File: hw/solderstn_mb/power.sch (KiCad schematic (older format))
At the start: 63 parts, among them Q301 Si4497DY, Q302 DMG1012T, U301 TPS54332DDA, U302 TLV1117LV30DCY, U303 TLV1117LV30DCY, U304 TLV1117LV30DCY, U305 AP22811AW5

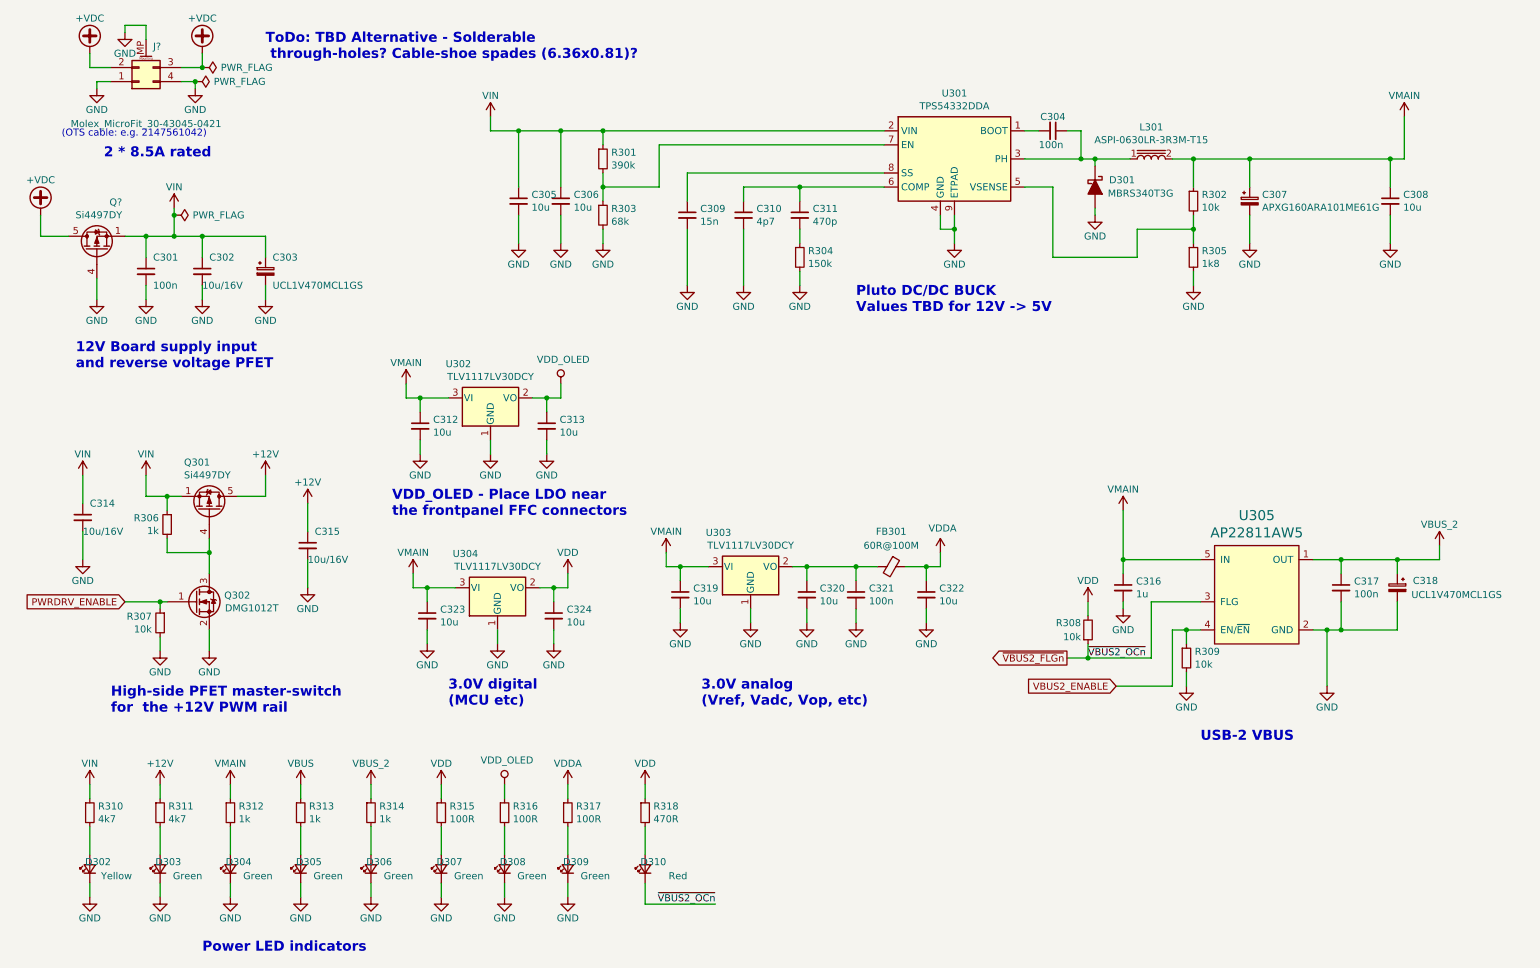
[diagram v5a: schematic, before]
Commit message: Updated display-board sch & PCB with optional left-hand rotary encoder instead of pwrbtn. Printed MB schematic updates PDF for 20-08-21
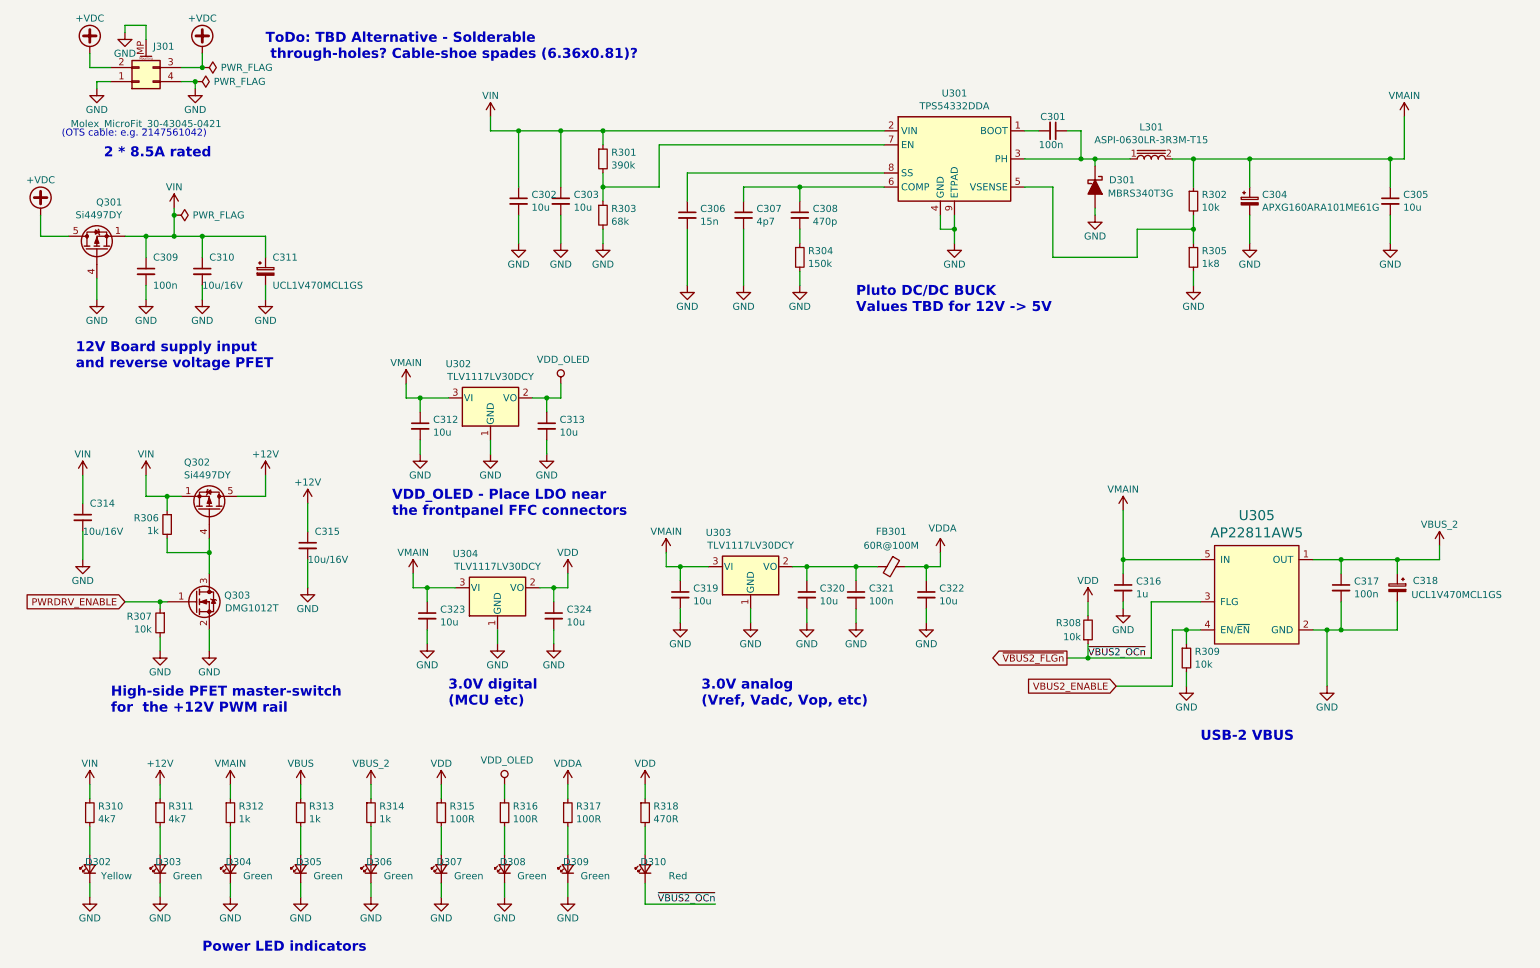
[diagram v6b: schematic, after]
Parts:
- gave numbers to parts that had none: 2
- renumbered C304 to C301, C305 to C302, C306 to C303, C307 to C304, C308 to C305, C309 to C306, C310 to C307, C311 to C308, C301 to C309, C302 to C310, C303 to C311, Q301 to Q302, Q302 to Q303

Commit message: Corrected several ERC issues. Re-annotated & assigned all footprints except 32k xtal (will prob. replace with RTC module anyway)
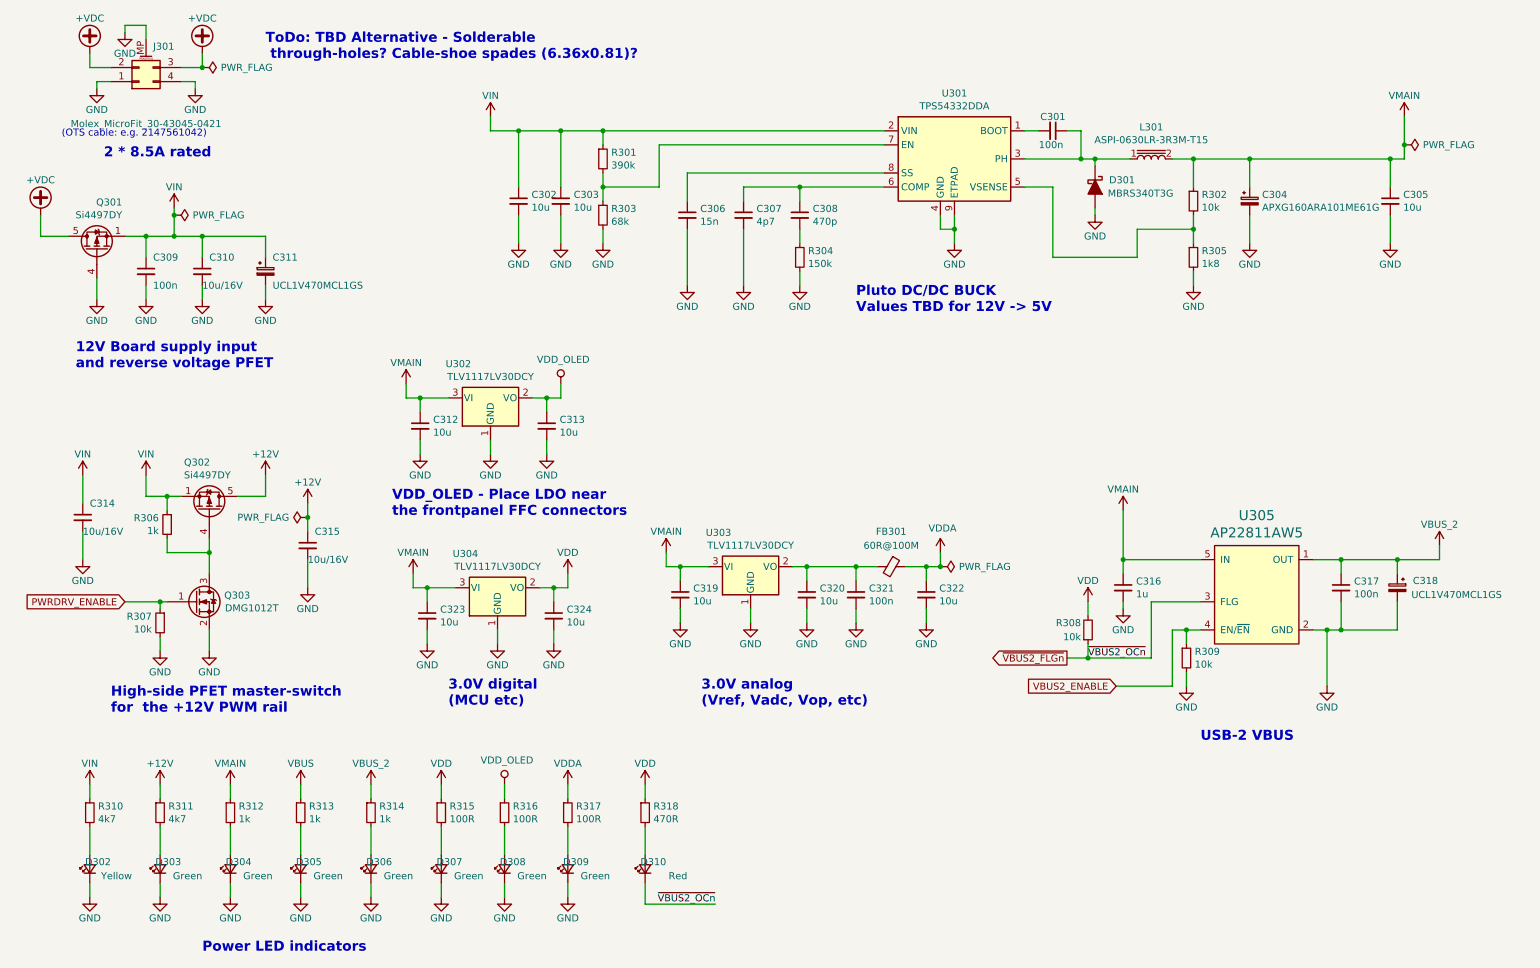
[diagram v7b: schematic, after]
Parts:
- C301, C302, C303, C305, C309, C310, C312, C313, C314, C315, C316, C317, C319, C320, C321, C322, C323, C324: footprint (none) -> Capacitor_SMD:C_0603_1608Metric
- C306, C307, C308: footprint (none) -> Capacitor_SMD:C_0402_1005Metric
- D302, D303, D304, D305, D306, D307, D308, D309, D310: footprint (none) -> LED_SMD:LED_0603_1608Metric
- FB301: footprint (none) -> Inductor_SMD:L_0603_1608Metric
- Q303: footprint bobs:SOT-523 -> customlib_mj_fp:SOT-523
- R301, R302, R303, R304, R305, R306, R307, R308, R309, R310, R311, R312, R313, R314, R315, R316, R317, R318: footprint (none) -> Resistor_SMD:R_0603_1608Metric

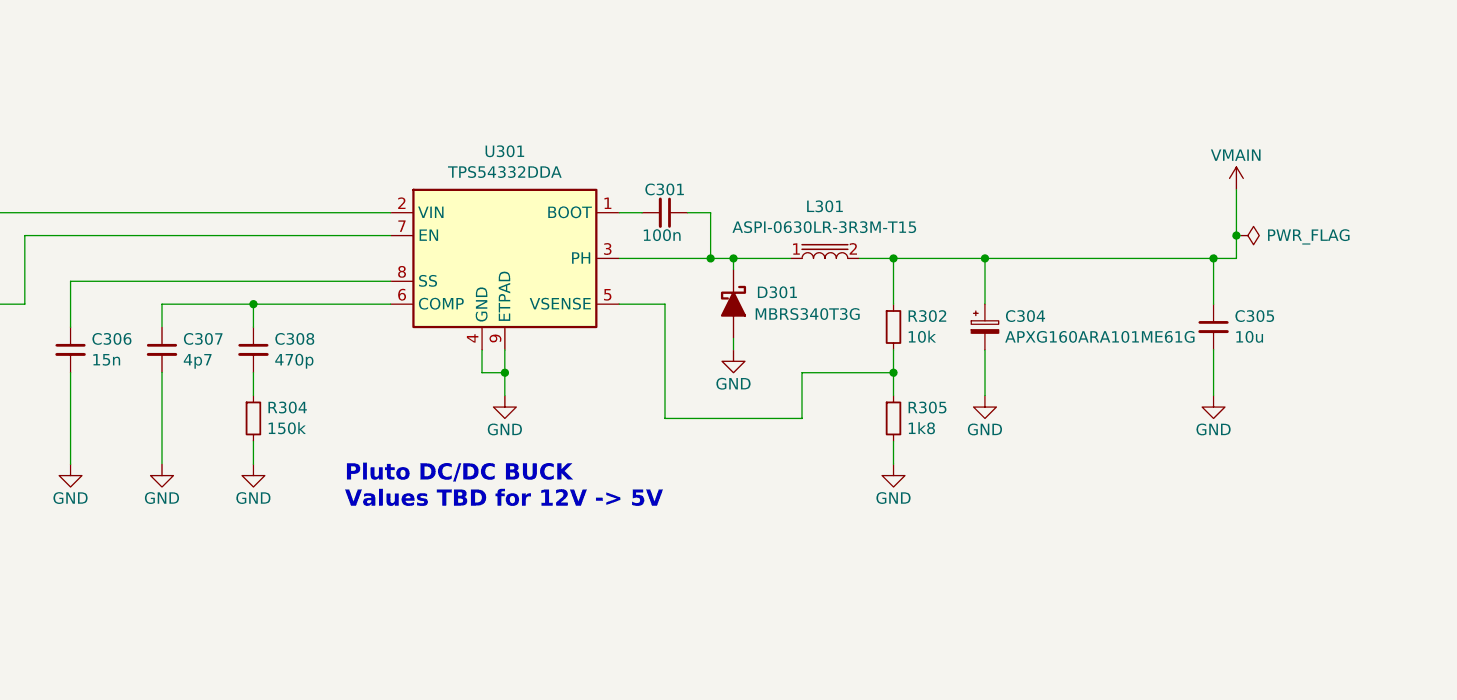
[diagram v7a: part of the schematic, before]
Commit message: Updated DC/DC buck values after testing TPS54332 in TI WebBench. New MB printed schematics.
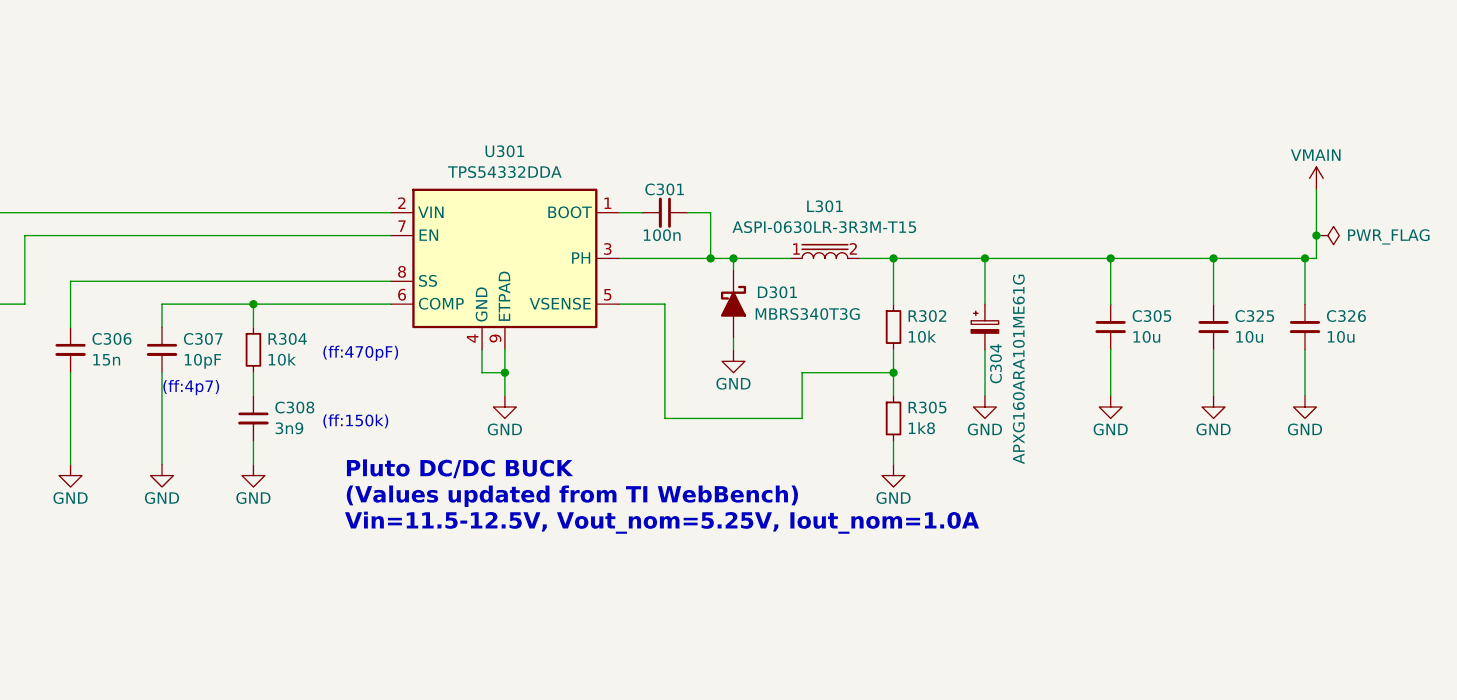
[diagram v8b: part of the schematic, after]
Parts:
- added C325, C326: 10u, Capacitor_SMD:C_0603_1608Metric, symbol Device:C_Small
- C307: value 4p7 -> 10pF
- C308: value 470p -> 3n9
- R304: value 150k -> 10k
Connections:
- net GND: now also C308.2, C325.2, C326.2; no longer R304.2
- net VMAIN: now also C325.1, C326.1
- net at C307.1, U301.6 (COMP): now also R304.1; no longer C308.1
- new net: C308.1, R304.2
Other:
- note added: "(ff:150k)"
- note added: "(ff:470pF)"
- note added: "(ff:4p7)"
- note added: "Pluto DC/DC BUCK\n(Values updated from TI WebBench)\nVin=11.5-12.5V, Vout_nom=5.25V, Iout_nom=1.0A"
- note removed: "Pluto DC/DC BUCK\nValues TBD for 12V -> 5V"
- moved on the sheet: C305, C308, R304
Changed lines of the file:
@@
 P 5650 2050
 F 0 "C307" H 5742 2096 50  0000 L CNN
-F 1 "4p7" H 5742 2005 50  0000 L CNN
+F 1 "10pF" H 5742 2005 50  0000 L CNN
 F 2 "Capacitor_SMD:C_0402_1005Metric" H 5650 2050 50  0001 C CNN
 F 3 "~" H 5650 2050 50  0001 C CNN
@@
 $EndComp
 $Comp
-L Device:C_Small C308
-U 1 1 5F4831B5
+L Device:R_Small R304
+U 1 1 5F483485
 P 6050 2050
-F 0 "C308" H 6142 2096 50  0000 L CNN
-F 1 "470p" H 6142 2005 50  0000 L CNN
-F 2 "Capacitor_SMD:C_0402_1005Metric" H 6050 2050 50  0001 C CNN
+F 0 "R304" H 6109 2096 50  0000 L CNN
+F 1 "10k" H 6109 2005 50  0000 L CNN
+F 2 "Resistor_SMD:R_0603_1608Metric" H 6050 2050 50  0001 C CNN
 F 3 "~" H 6050 2050 50  0001 C CNN
 	1    6050 2050
-	1    0    0    -1
-$EndComp
-$Comp
-L Device:R_Small R304
-U 1 1 5F483485
-P 6050 2350
-F 0 "R304" H 6109 2396 50  0000 L CNN
-F 1 "150k" H 6109 2305 50  0000 L CNN
-F 2 "Resistor_SMD:R_0603_1608Metric" H 6050 2350 50  0001 C CNN
-F 3 "~" H 6050 2350 50  0001 C CNN
-	1    6050 2350
 	1    0    0    -1
 $EndComp
@@
 	5650 1850 5650 1950
 Connection ~ 6050 1850
-Wire Wire Line
-	6050 2150 6050 2250
 Wire Wire Line
 	6650 1750 5250 1750
@@
 U 1 1 5F497049
 P 9250 1950
-F 0 "C304" H 9338 1996 50  0000 L CNN
-F 1 "APXG160ARA101ME61G" H 9338 1905 50  0000 L CNN
+F 0 "C304" V 9300 1700 50  0000 L CNN
+F 1 "APXG160ARA101ME61G" V 9400 1350 50  0000 L CNN
 F 2 "Capacitor_SMD:CP_Elec_5x5.8" H 9250 1950 50  0001 C CNN
 F 3 "https://www.mouser.se/datasheet/2/420/United-Chemi-Con-775864.pdf" H 9250 1950 50  0001 C CNN
@@
 L Device:C_Small C305
 U 1 1 5F497D32
-P 10250 1950
-F 0 "C305" H 10342 1996 50  0000 L CNN
-F 1 "10u" H 10342 1905 50  0000 L CNN
-F 2 "Capacitor_SMD:C_0603_1608Metric" H 10250 1950 50  0001 C CNN
-F 3 "~" H 10250 1950 50  0001 C CNN
-	1    10250 1950
+P 9800 1950
+F 0 "C305" H 9892 1996 50  0000 L CNN
+F 1 "10u" H 9892 1905 50  0000 L CNN
+F 2 "Capacitor_SMD:C_0603_1608Metric" H 9800 1950 50  0001 C CNN
+F 3 "~" H 9800 1950 50  0001 C CNN
+	1    9800 1950
 	1    0    0    -1
 $EndComp
@@
 L power:GND #PWR0316
 U 1 1 5F499E9F
-P 10250 2250
-F 0 "#PWR0316" H 10250 2000 50  0001 C CNN
-F 1 "GND" H 10250 2100 50  0000 C CNN
-F 2 "" H 10250 2250 50  0001 C CNN
-F 3 "" H 10250 2250 50  0001 C CNN
-	1    10250 2250
+P 9800 2250
+F 0 "#PWR0316" H 9800 2000 50  0001 C CNN
+F 1 "GND" H 9800 2100 50  0000 C CNN
+F 2 "" H 9800 2250 50  0001 C CNN
+F 3 "" H 9800 2250 50  0001 C CNN
+	1    9800 2250
 	1    0    0    -1
 $EndComp
@@
 L customlib_mj:VMAIN #PWR0307
 U 1 1 5F4A6151
-P 10350 1350
-F 0 "#PWR0307" H 10350 1200 50  0001 C CNN
-F 1 "VMAIN" H 10350 1500 50  0000 C CNN
-F 2 "" H 10350 1350 50  0001 C CNN
-F 3 "" H 10350 1350 50  0001 C CNN
-	1    10350 1350
+P 10700 1350
+F 0 "#PWR0307" H 10700 1200 50  0001 C CNN
+F 1 "VMAIN" H 10700 1500 50  0000 C CNN
+F 2 "" H 10700 1350 50  0001 C CNN
+F 3 "" H 10700 1350 50  0001 C CNN
+	1    10700 1350
 	1    0    0    -1
 $EndComp
@@
 	8700 1650 8850 1650
 Wire Wire Line
-	10350 1650 10350 1550
+	10700 1650 10700 1550
 Wire Wire Line
 	8850 1850 8850 1650
@@
 Connection ~ 9250 1650
 Wire Wire Line
-	9250 1650 10250 1650
+	9250 1650 9800 1650
 Wire Wire Line
 	9250 2250 9250 2050
 Wire Wire Line
-	10250 2250 10250 2050
-Wire Wire Line
-	10250 1850 10250 1650
-Connection ~ 10250 1650
-Wire Wire Line
-	10250 1650 10350 1650
-Text Notes 6450 2750 0    71   ~ 14
-Pluto DC/DC BUCK\nValues TBD for 12V -> 5V
+	9800 2250 9800 2050
+Wire Wire Line
+	9800 1850 9800 1650
+Text Notes 6450 2850 0    71   ~ 14
+Pluto DC/DC BUCK\n(Values updated from TI WebBench)\nVin=11.5-12.5V, Vout_nom=5.25V, Iout_nom=1.0A
 $Comp
 L customlib_mj:TLV1117LV30DCY U304
@@
 L power:PWR_FLAG #FLG0302
 U 1 1 5F505787
-P 10350 1550
-F 0 "#FLG0302" H 10350 1625 50  0001 C CNN
-F 1 "PWR_FLAG" V 10350 1866 50  0000 C CNN
-F 2 "" H 10350 1550 50  0001 C CNN
-F 3 "~" H 10350 1550 50  0001 C CNN
-	1    10350 1550
+P 10700 1550
+F 0 "#FLG0302" H 10700 1625 50  0001 C CNN
+F 1 "PWR_FLAG" V 10700 1866 50  0000 C CNN
+F 2 "" H 10700 1550 50  0001 C CNN
+F 3 "~" H 10700 1550 50  0001 C CNN
+	1    10700 1550
 	0    1    1    0
 $EndComp
-Connection ~ 10350 1550
-Wire Wire Line
-	10350 1550 10350 1350
+Connection ~ 10700 1550
+Wire Wire Line
+	10700 1550 10700 1350
 $Comp
 L power:PWR_FLAG #FLG0304
@@
 Wire Wire Line
 	2550 4200 2550 4300
+Text Notes 5650 2250 0    50   ~ 0
+(ff:4p7)
+Text Notes 6350 2400 0    50   ~ 0
+(ff:150k)
+$Comp
+L Device:C_Small C308
+U 1 1 5F4831B5
+P 6050 2350
+F 0 "C308" H 6142 2396 50  0000 L CNN
+F 1 "3n9" H 6142 2305 50  0000 L CNN
+F 2 "Capacitor_SMD:C_0402_1005Metric" H 6050 2350 50  0001 C CNN
+F 3 "~" H 6050 2350 50  0001 C CNN
+	1    6050 2350
+	1    0    0    -1
+$EndComp
+Text Notes 6350 2100 0    50   ~ 0
+(ff:470pF)
+Wire Wire Line
+	6050 2250 6050 2150
+Connection ~ 9800 1650
+$Comp
+L Device:C_Small C325
+U 1 1 5F4B09C1
+P 10250 1950
+F 0 "C325" H 10342 1996 50  0000 L CNN
+F 1 "10u" H 10342 1905 50  0000 L CNN
+F 2 "Capacitor_SMD:C_0603_1608Metric" H 10250 1950 50  0001 C CNN
+F 3 "~" H 10250 1950 50  0001 C CNN
+	1    10250 1950
+	1    0    0    -1
+$EndComp
+$Comp
+L power:GND #PWR0373
+U 1 1 5F4B09CB
+P 10250 2250
+F 0 "#PWR0373" H 10250 2000 50  0001 C CNN
+F 1 "GND" H 10250 2100 50  0000 C CNN
+F 2 "" H 10250 2250 50  0001 C CNN
+F 3 "" H 10250 2250 50  0001 C CNN
+	1    10250 2250
+	1    0    0    -1
+$EndComp
+Wire Wire Line
+	10250 2250 10250 2050
+Wire Wire Line
+	10250 1850 10250 1650
+$Comp
+L Device:C_Small C326
+U 1 1 5F4BEE07
+P 10650 1950
+F 0 "C326" H 10742 1996 50  0000 L CNN
+F 1 "10u" H 10742 1905 50  0000 L CNN
+F 2 "Capacitor_SMD:C_0603_1608Metric" H 10650 1950 50  0001 C CNN
+F 3 "~" H 10650 1950 50  0001 C CNN
+	1    10650 1950
+	1    0    0    -1
+$EndComp
+$Comp
+L power:GND #PWR0374
+U 1 1 5F4BEE11
+P 10650 2250
+F 0 "#PWR0374" H 10650 2000 50  0001 C CNN
+F 1 "GND" H 10650 2100 50  0000 C CNN
+F 2 "" H 10650 2250 50  0001 C CNN
+F 3 "" H 10650 2250 50  0001 C CNN
+	1    10650 2250
+	1    0    0    -1
+$EndComp
+Wire Wire Line
+	10650 2250 10650 2050
+Wire Wire Line
+	10650 1850 10650 1650
+Connection ~ 10650 1650
+Wire Wire Line
+	10650 1650 10700 1650
+Connection ~ 10250 1650
+Wire Wire Line
+	10250 1650 10650 1650
+Wire Wire Line
+	9800 1650 10250 1650
 $EndSCHEMATC
